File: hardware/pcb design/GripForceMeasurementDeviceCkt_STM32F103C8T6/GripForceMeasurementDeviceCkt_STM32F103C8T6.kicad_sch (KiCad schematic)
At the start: 25 parts, among them J1 Conn_01x03, P1 USB_C_Plug_USB2.0, U1 STM32F103C8Tx, U2 FT232RL, Y1 8MHz

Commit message: initial design of schemetic has completed
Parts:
- removed J1: Conn_01x03, symbol Connector_Generic:Conn_01x03
- added C15, C16, C17, C18, C19, C20, C21, C22, C23, C24: 100n, Capacitor_SMD:C_0603_1608Metric, symbol Device:C
- added J1, J10, J11, J12, J13, J5, J6, J7, J8, J9: Conn_01x32, Connector_FFC-FPC:TE_3-1734839-2_1x32-1MP_P0.5mm_Horizontal, symbol Connector_Generic:Conn_01x32
- added J2: Conn_01x03, Connector_PinHeader_2.54mm:PinHeader_1x03_P2.54mm_Vertical, symbol Connector_Generic:Conn_01x03
- added J3: Conn_01x04, Connector_PinHeader_2.54mm:PinHeader_1x04_P2.54mm_Vertical, symbol Connector_Generic:Conn_01x04
- added J4: Conn_02x03_CC, Connector_PinHeader_2.54mm:PinHeader_2x03_P2.54mm_Vertical, symbol Connector_Generic:Conn_02x03_Counter_Clockwise
- added R4: 330R, Resistor_THT:R_Axial_DIN0207_L6.3mm_D2.5mm_P7.62mm_Horizontal, symbol Device:R
- added RV1: 500k, Potentiometer_THT:Potentiometer_Bourns_3296W_Vertical, symbol Device:R_Potentiometer
- added U10, U11, U12, U13, U3, U4, U6, U7, U8, U9: ADG732BSUZ, Package_QFP:TQFP-48_7x7mm_P0.5mm, symbol ADG732BSUZ:ADG732BSUZ
- added U5: LM358, Package_SO:SO-8_3.9x4.9mm_P1.27mm, symbol Amplifier_Operational:LM358
- C1, C11, C14, C2, C3, C4, C5, C6, C7, C8: footprint (none) -> Capacitor_SMD:C_0603_1608Metric
- C10, C9: footprint (none) -> Capacitor_SMD:C_0402_1005Metric
- C12, C13: footprint (none) -> Capacitor_SMD:C_1206_3216Metric
- D1: footprint Diode_THT:D_DO-41_SOD81_P10.16mm_Horizontal -> Diode_SMD:D_MicroMELF
- FB1, L1: footprint (none) -> Inductor_SMD:L_0805_2012Metric
- P1: footprint (none) -> Connector_USB:USB_C_Receptacle_Amphenol_12401610E4-2A
- R1, R2, R3: footprint (none) -> Resistor_SMD:R_0603_1608Metric
- Y1: footprint (none) -> Crystal:Crystal_HC49-4H_Vertical
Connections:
- net +3.3V: now also J3.1 (Pin_1), J4.1 (Pin_1), J4.6 (Pin_6)
- net +5V: now also C15.1, C16.1, C17.1, C18.1, C19.1, C20.1, C21.1, C22.1, C23.1, C24.1, U10.13 (VDD), U10.14 (VDD)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
- net GND: now also C15.2, C16.2, C17.2, C18.2, C19.2, C20.2, C21.2, C22.2, C23.2, C24.2, J3.4 (Pin_4), J4.3 (Pin_3)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
- net SW_BOOT0: now also J4.5 (Pin_5)
- net ADC: now reaches U1.10 (PA0)
- net ADC: now also J2.2 (Pin_2)
- net COL_SEL_R_3: now reaches U1.11 (PA1)
- net COL_SEL_R_3: now also U12.20 (~{CS})
- net COL_SEL_R_4: now reaches U1.12 (PA2)
- net COL_SEL_R_4: now also U13.20 (~{CS})
- net GYRO_SELECT: now reaches U1.13 (PA3)
- net NSS: now reaches U1.14 (PA4)
- net SCK: now reaches U1.15 (PA5)
- net MISO: now reaches U1.16 (PA6)
- net MOSI: now reaches U1.17 (PA7)
- net ROW_SEL_L: now reaches U1.18 (PB0)
- net ROW_SEL_L: now also U3.20 (~{CS})
- net ROW_SEL_R: now reaches U1.19 (PB1)
- net ROW_SEL_R: now also U4.20 (~{CS})
- net BOOT1: now reaches U1.20 (PB2)
- net BOOT1: now also J4.2 (Pin_2)
- net COL_SEL_L_1: now reaches U1.21 (PB10)
- net COL_SEL_L_1: now also U6.20 (~{CS})
- net COL_SEL_L_2: now reaches U1.22 (PB11)
- net COL_SEL_L_2: now also U7.20 (~{CS})
- net COL_SEL_L_3: now reaches U1.25 (PB12)
- net COL_SEL_L_3: now also U8.20 (~{CS})
- net COL_SEL_L_4: now reaches U1.26 (PB13)
- net COL_SEL_L_4: now also U9.20 (~{CS})
- net COL_SEL_R_1: now reaches U1.27 (PB14)
- net COL_SEL_R_1: now also U10.20 (~{CS})
- net COL_SEL_R_2: now reaches U1.28 (PB15)
- net COL_SEL_R_2: now also U11.20 (~{CS})
- net ESP_SELECT: now reaches U1.29 (PA8)
- net at U1.34 (PA13): now also J3.2 (Pin_2)
- net at U1.37 (PA14): now also J3.3 (Pin_3)
- net ADG_WR: now reaches U1.39 (PB3)
- net ADG_WR: now also U10.21 (~{WR}), U11.21 (~{WR}), U12.21 (~{WR}), U13.21 (~{WR}), U3.21 (~{WR}), U4.21 (~{WR}), U6.21 (~{WR}), U7.21 (~{WR}), U8.21 (~{WR}), U9.21 (~{WR})
- net ADG_EN: now reaches U1.40 (PB4)
- net ADG_EN: now also U10.22 (~{EN}), U11.22 (~{EN}), U12.22 (~{EN}), U13.22 (~{EN}), U3.22 (~{EN}), U4.22 (~{EN}), U6.22 (~{EN}), U7.22 (~{EN}), U8.22 (~{EN}), U9.22 (~{EN})
- net L0: now reaches U1.41 (PB5)
- net L0: now also U10.15 (A0), U11.15 (A0), U12.15 (A0), U13.15 (A0), U3.15 (A0), U4.15 (A0), U6.15 (A0), U7.15 (A0), U8.15 (A0), U9.15 (A0)
- net L1: now reaches U1.42 (PB6)
- net L1: now also U10.16 (A1), U11.16 (A1), U12.16 (A1), U13.16 (A1), U3.16 (A1), U4.16 (A1), U6.16 (A1), U7.16 (A1), U8.16 (A1), U9.16 (A1)
- net L2: now reaches U1.43 (PB7)
- net L2: now also U10.17 (A2), U11.17 (A2), U12.17 (A2), U13.17 (A2), U3.17 (A2), U4.17 (A2), U6.17 (A2), U7.17 (A2), U8.17 (A2), U9.17 (A2)
- net L3: now reaches U1.45 (PB8)
- net L3: now also U10.18 (A3), U11.18 (A3), U12.18 (A3), U13.18 (A3), U3.18 (A3), U4.18 (A3), U6.18 (A3), U7.18 (A3), U8.18 (A3), U9.18 (A3)
- net L4: now reaches U1.46 (PB9)
- net L4: now also U10.19 (A4), U11.19 (A4), U12.19 (A4), U13.19 (A4), U3.19 (A4), U4.19 (A4), U6.19 (A4), U7.19 (A4), U8.19 (A4), U9.19 (A4)
- new net: J2.1 (Pin_1), RV1.1, U5.7
- new net: RV1.2, U5.6 (-)
- new net: J2.3 (Pin_3), U5.1, U5.2 (-), U5.5 (+)
- new net COL_L_1.S1: J5.32 (Pin_32), U6.12 (S1)
- new net COL_L_1.S10: J5.23 (Pin_23), U6.3 (S10)
- new net COL_L_1.S11: J5.22 (Pin_22), U6.2 (S11)
- new net COL_L_1.S12: J5.21 (Pin_21), U6.1 (S12)
- new net COL_L_1.S13: J5.20 (Pin_20), U6.48 (S13)
- new net COL_L_1.S14: J5.19 (Pin_19), U6.47 (S14)
- new net COL_L_1.S15: J5.18 (Pin_18), U6.46 (S15)
- new net COL_L_1.S16: J5.17 (Pin_17), U6.45 (S16)
- new net COL_L_1.S17: J5.1 (Pin_1), U6.25 (S17)
- new net COL_L_1.S18: J5.2 (Pin_2), U6.26 (S18)
- new net COL_L_1.S19: J5.3 (Pin_3), U6.27 (S19)
- new net COL_L_1.S2: J5.31 (Pin_31), U6.11 (S2)
- new net COL_L_1.S20: J5.4 (Pin_4), U6.28 (S20)
- new net COL_L_1.S21: J5.5 (Pin_5), U6.29 (S21)
- new net COL_L_1.S22: J5.6 (Pin_6), U6.30 (S22)
- new net COL_L_1.S23: J5.7 (Pin_7), U6.31 (S23)
- new net COL_L_1.S24: J5.8 (Pin_8), U6.32 (S24)
- new net COL_L_1.S25: J5.9 (Pin_9), U6.33 (S25)
- new net COL_L_1.S26: J5.10 (Pin_10), U6.34 (S26)
- new net COL_L_1.S27: J5.11 (Pin_11), U6.35 (S27)
- new net COL_L_1.S28: J5.12 (Pin_12), U6.36 (S28)
- new net COL_L_1.S29: J5.13 (Pin_13), U6.37 (S29)
- new net COL_L_1.S3: J5.30 (Pin_30), U6.10 (S3)
- new net COL_L_1.S30: J5.14 (Pin_14), U6.38 (S30)
- new net COL_L_1.S31: J5.15 (Pin_15), U6.39 (S31)
- new net COL_L_1.S32: J5.16 (Pin_16), U6.40 (S32)
- new net COL_L_1.S4: J5.29 (Pin_29), U6.9 (S4)
- new net COL_L_1.S5: J5.28 (Pin_28), U6.8 (S5)
- new net COL_L_1.S6: J5.27 (Pin_27), U6.7 (S6)
- new net COL_L_1.S7: J5.26 (Pin_26), U6.6 (S7)
- new net COL_L_1.S8: J5.25 (Pin_25), U6.5 (S8)
- new net COL_L_1.S9: J5.24 (Pin_24), U6.4 (S9)
- new net COL_L_2.S1: J6.1 (Pin_1), U7.12 (S1)
- new net COL_L_2.S10: J6.10 (Pin_10), U7.3 (S10)
- new net COL_L_2.S11: J6.11 (Pin_11), U7.2 (S11)
- new net COL_L_2.S12: J6.12 (Pin_12), U7.1 (S12)
- new net COL_L_2.S13: J6.13 (Pin_13), U7.48 (S13)
- new net COL_L_2.S14: J6.14 (Pin_14), U7.47 (S14)
- new net COL_L_2.S15: J6.15 (Pin_15), U7.46 (S15)
- new net COL_L_2.S16: J6.16 (Pin_16), U7.45 (S16)
- new net COL_L_2.S17: J6.32 (Pin_32), U7.25 (S17)
- new net COL_L_2.S18: J6.31 (Pin_31), U7.26 (S18)
- new net COL_L_2.S19: J6.30 (Pin_30), U7.27 (S19)
- new net COL_L_2.S2: J6.2 (Pin_2), U7.11 (S2)
- new net COL_L_2.S20: J6.29 (Pin_29), U7.28 (S20)
- new net COL_L_2.S21: J6.28 (Pin_28), U7.29 (S21)
- new net COL_L_2.S22: J6.27 (Pin_27), U7.30 (S22)
- new net COL_L_2.S23: J6.26 (Pin_26), U7.31 (S23)
- new net COL_L_2.S24: J6.25 (Pin_25), U7.32 (S24)
- new net COL_L_2.S25: J6.24 (Pin_24), U7.33 (S25)
- new net COL_L_2.S26: J6.23 (Pin_23), U7.34 (S26)
- new net COL_L_2.S27: J6.22 (Pin_22), U7.35 (S27)
- new net COL_L_2.S28: J6.21 (Pin_21), U7.36 (S28)
- new net COL_L_2.S29: J6.20 (Pin_20), U7.37 (S29)
- new net COL_L_2.S3: J6.3 (Pin_3), U7.10 (S3)
- new net COL_L_2.S30: J6.19 (Pin_19), U7.38 (S30)
- new net COL_L_2.S31: J6.18 (Pin_18), U7.39 (S31)
- new net COL_L_2.S32: J6.17 (Pin_17), U7.40 (S32)
- new net COL_L_2.S4: J6.4 (Pin_4), U7.9 (S4)
- new net COL_L_2.S5: J6.5 (Pin_5), U7.8 (S5)
- new net COL_L_2.S6: J6.6 (Pin_6), U7.7 (S6)
- new net COL_L_2.S7: J6.7 (Pin_7), U7.6 (S7)
- new net COL_L_2.S8: J6.8 (Pin_8), U7.5 (S8)
- new net COL_L_2.S9: J6.9 (Pin_9), U7.4 (S9)
- new net COL_L_3.S1: J7.1 (Pin_1), U8.12 (S1)
- new net COL_L_3.S10: J7.10 (Pin_10), U8.3 (S10)
- new net COL_L_3.S11: J7.11 (Pin_11), U8.2 (S11)
- new net COL_L_3.S12: J7.12 (Pin_12), U8.1 (S12)
- new net COL_L_3.S13: J7.13 (Pin_13), U8.48 (S13)
- new net COL_L_3.S14: J7.14 (Pin_14), U8.47 (S14)
- new net COL_L_3.S15: J7.15 (Pin_15), U8.46 (S15)
- new net COL_L_3.S16: J7.16 (Pin_16), U8.45 (S16)
- new net COL_L_3.S17: J7.32 (Pin_32), U8.25 (S17)
- new net COL_L_3.S18: J7.31 (Pin_31), U8.26 (S18)
- new net COL_L_3.S19: J7.30 (Pin_30), U8.27 (S19)
- new net COL_L_3.S2: J7.2 (Pin_2), U8.11 (S2)
- new net COL_L_3.S20: J7.29 (Pin_29), U8.28 (S20)
- new net COL_L_3.S21: J7.28 (Pin_28), U8.29 (S21)
- new net COL_L_3.S22: J7.27 (Pin_27), U8.30 (S22)
- new net COL_L_3.S23: J7.26 (Pin_26), U8.31 (S23)
- new net COL_L_3.S24: J7.25 (Pin_25), U8.32 (S24)
- new net COL_L_3.S25: J7.24 (Pin_24), U8.33 (S25)
- new net COL_L_3.S26: J7.23 (Pin_23), U8.34 (S26)
- new net COL_L_3.S27: J7.22 (Pin_22), U8.35 (S27)
- new net COL_L_3.S28: J7.21 (Pin_21), U8.36 (S28)
- new net COL_L_3.S29: J7.20 (Pin_20), U8.37 (S29)
- new net COL_L_3.S3: J7.3 (Pin_3), U8.10 (S3)
- new net COL_L_3.S30: J7.19 (Pin_19), U8.38 (S30)
- new net COL_L_3.S31: J7.18 (Pin_18), U8.39 (S31)
- new net COL_L_3.S32: J7.17 (Pin_17), U8.40 (S32)
- new net COL_L_3.S4: J7.4 (Pin_4), U8.9 (S4)
- new net COL_L_3.S5: J7.5 (Pin_5), U8.8 (S5)
- new net COL_L_3.S6: J7.6 (Pin_6), U8.7 (S6)
- new net COL_L_3.S7: J7.7 (Pin_7), U8.6 (S7)
- new net COL_L_3.S8: J7.8 (Pin_8), U8.5 (S8)
- new net COL_L_3.S9: J7.9 (Pin_9), U8.4 (S9)
- new net COL_L_4.S1: J8.1 (Pin_1), U9.12 (S1)
- new net COL_L_4.S10: J8.10 (Pin_10), U9.3 (S10)
- new net COL_L_4.S11: J8.11 (Pin_11), U9.2 (S11)
- new net COL_L_4.S12: J8.12 (Pin_12), U9.1 (S12)
- new net COL_L_4.S13: J8.13 (Pin_13), U9.48 (S13)
- new net COL_L_4.S14: J8.14 (Pin_14), U9.47 (S14)
- new net COL_L_4.S15: J8.15 (Pin_15), U9.46 (S15)
- new net COL_L_4.S16: J8.16 (Pin_16), U9.45 (S16)
- new net COL_L_4.S17: J8.32 (Pin_32), U9.25 (S17)
- new net COL_L_4.S18: J8.31 (Pin_31), U9.26 (S18)
- new net COL_L_4.S19: J8.30 (Pin_30), U9.27 (S19)
- new net COL_L_4.S2: J8.2 (Pin_2), U9.11 (S2)
- new net COL_L_4.S20: J8.29 (Pin_29), U9.28 (S20)
- new net COL_L_4.S21: J8.28 (Pin_28), U9.29 (S21)
- new net COL_L_4.S22: J8.27 (Pin_27), U9.30 (S22)
- new net COL_L_4.S23: J8.26 (Pin_26), U9.31 (S23)
- new net COL_L_4.S24: J8.25 (Pin_25), U9.32 (S24)
- new net COL_L_4.S25: J8.24 (Pin_24), U9.33 (S25)
- new net COL_L_4.S26: J8.23 (Pin_23), U9.34 (S26)
- new net COL_L_4.S27: J8.22 (Pin_22), U9.35 (S27)
- new net COL_L_4.S28: J8.21 (Pin_21), U9.36 (S28)
- new net COL_L_4.S29: J8.20 (Pin_20), U9.37 (S29)
- new net COL_L_4.S3: J8.3 (Pin_3), U9.10 (S3)
- new net COL_L_4.S30: J8.19 (Pin_19), U9.38 (S30)
- new net COL_L_4.S31: J8.18 (Pin_18), U9.39 (S31)
- new net COL_L_4.S32: J8.17 (Pin_17), U9.40 (S32)
- new net COL_L_4.S4: J8.4 (Pin_4), U9.9 (S4)
- new net COL_L_4.S5: J8.5 (Pin_5), U9.8 (S5)
- new net COL_L_4.S6: J8.6 (Pin_6), U9.7 (S6)
- new net COL_L_4.S7: J8.7 (Pin_7), U9.6 (S7)
- new net COL_L_4.S8: J8.8 (Pin_8), U9.5 (S8)
- new net COL_L_4.S9: J8.9 (Pin_9), U9.4 (S9)
- new net COL_R_1.S1: J9.1 (Pin_1), U10.12 (S1)
- new net COL_R_1.S10: J9.10 (Pin_10), U10.3 (S10)
- new net COL_R_1.S11: J9.11 (Pin_11), U10.2 (S11)
- new net COL_R_1.S12: J9.12 (Pin_12), U10.1 (S12)
- new net COL_R_1.S13: J9.13 (Pin_13), U10.48 (S13)
- new net COL_R_1.S14: J9.14 (Pin_14), U10.47 (S14)
- new net COL_R_1.S15: J9.15 (Pin_15), U10.46 (S15)
- new net COL_R_1.S16: J9.16 (Pin_16), U10.45 (S16)
- new net COL_R_1.S17: J9.32 (Pin_32), U10.25 (S17)
- new net COL_R_1.S18: J9.31 (Pin_31), U10.26 (S18)
- new net COL_R_1.S19: J9.30 (Pin_30), U10.27 (S19)
- new net COL_R_1.S2: J9.2 (Pin_2), U10.11 (S2)
- new net COL_R_1.S20: J9.29 (Pin_29), U10.28 (S20)
- new net COL_R_1.S21: J9.28 (Pin_28), U10.29 (S21)
- new net COL_R_1.S22: J9.27 (Pin_27), U10.30 (S22)
- new net COL_R_1.S23: J9.26 (Pin_26), U10.31 (S23)
- new net COL_R_1.S24: J9.25 (Pin_25), U10.32 (S24)
- new net COL_R_1.S25: J9.24 (Pin_24), U10.33 (S25)
- new net COL_R_1.S26: J9.23 (Pin_23), U10.34 (S26)
- new net COL_R_1.S27: J9.22 (Pin_22), U10.35 (S27)
- new net COL_R_1.S28: J9.21 (Pin_21), U10.36 (S28)
- new net COL_R_1.S29: J9.20 (Pin_20), U10.37 (S29)
- new net COL_R_1.S3: J9.3 (Pin_3), U10.10 (S3)
- new net COL_R_1.S30: J9.19 (Pin_19), U10.38 (S30)
- new net COL_R_1.S31: J9.18 (Pin_18), U10.39 (S31)
- new net COL_R_1.S32: J9.17 (Pin_17), U10.40 (S32)
- new net COL_R_1.S4: J9.4 (Pin_4), U10.9 (S4)
- new net COL_R_1.S5: J9.5 (Pin_5), U10.8 (S5)
- new net COL_R_1.S6: J9.6 (Pin_6), U10.7 (S6)
- new net COL_R_1.S7: J9.7 (Pin_7), U10.6 (S7)
- new net COL_R_1.S8: J9.8 (Pin_8), U10.5 (S8)
- new net COL_R_1.S9: J9.9 (Pin_9), U10.4 (S9)
- new net COL_R_2.S1: J11.1 (Pin_1), U11.12 (S1)
- new net COL_R_2.S10: J11.10 (Pin_10), U11.3 (S10)
- new net COL_R_2.S11: J11.11 (Pin_11), U11.2 (S11)
- new net COL_R_2.S12: J11.12 (Pin_12), U11.1 (S12)
- new net COL_R_2.S13: J11.13 (Pin_13), U11.48 (S13)
- new net COL_R_2.S14: J11.14 (Pin_14), U11.47 (S14)
- new net COL_R_2.S15: J11.15 (Pin_15), U11.46 (S15)
- new net COL_R_2.S16: J11.16 (Pin_16), U11.45 (S16)
- new net COL_R_2.S17: J11.32 (Pin_32), U11.25 (S17)
- new net COL_R_2.S18: J11.31 (Pin_31), U11.26 (S18)
- new net COL_R_2.S19: J11.30 (Pin_30), U11.27 (S19)
- new net COL_R_2.S2: J11.2 (Pin_2), U11.11 (S2)
- new net COL_R_2.S20: J11.29 (Pin_29), U11.28 (S20)
- new net COL_R_2.S21: J11.28 (Pin_28), U11.29 (S21)
- new net COL_R_2.S22: J11.27 (Pin_27), U11.30 (S22)
- new net COL_R_2.S23: J11.26 (Pin_26), U11.31 (S23)
- new net COL_R_2.S24: J11.25 (Pin_25), U11.32 (S24)
- new net COL_R_2.S25: J11.24 (Pin_24), U11.33 (S25)
- new net COL_R_2.S26: J11.23 (Pin_23), U11.34 (S26)
- new net COL_R_2.S27: J11.22 (Pin_22), U11.35 (S27)
- new net COL_R_2.S28: J11.21 (Pin_21), U11.36 (S28)
- new net COL_R_2.S29: J11.20 (Pin_20), U11.37 (S29)
- new net COL_R_2.S3: J11.3 (Pin_3), U11.10 (S3)
- new net COL_R_2.S30: J11.19 (Pin_19), U11.38 (S30)
- new net COL_R_2.S31: J11.18 (Pin_18), U11.39 (S31)
- new net COL_R_2.S32: J11.17 (Pin_17), U11.40 (S32)
- new net COL_R_2.S4: J11.4 (Pin_4), U11.9 (S4)
- new net COL_R_2.S5: J11.5 (Pin_5), U11.8 (S5)
- new net COL_R_2.S6: J11.6 (Pin_6), U11.7 (S6)
- new net COL_R_2.S7: J11.7 (Pin_7), U11.6 (S7)
- new net COL_R_2.S8: J11.8 (Pin_8), U11.5 (S8)
- new net COL_R_2.S9: J11.9 (Pin_9), U11.4 (S9)
- new net COL_R_3.S1: J12.1 (Pin_1), U12.12 (S1)
- new net COL_R_3.S10: J12.10 (Pin_10), U12.3 (S10)
- new net COL_R_3.S11: J12.11 (Pin_11), U12.2 (S11)
- new net COL_R_3.S12: J12.12 (Pin_12), U12.1 (S12)
- new net COL_R_3.S13: J12.13 (Pin_13), U12.48 (S13)
- new net COL_R_3.S14: J12.14 (Pin_14), U12.47 (S14)
- new net COL_R_3.S15: J12.15 (Pin_15), U12.46 (S15)
- new net COL_R_3.S16: J12.16 (Pin_16), U12.45 (S16)
- new net COL_R_3.S17: J12.32 (Pin_32), U12.25 (S17)
- new net COL_R_3.S18: J12.31 (Pin_31), U12.26 (S18)
- new net COL_R_3.S19: J12.30 (Pin_30), U12.27 (S19)
- new net COL_R_3.S2: J12.2 (Pin_2), U12.11 (S2)
- new net COL_R_3.S20: J12.29 (Pin_29), U12.28 (S20)
- new net COL_R_3.S21: J12.28 (Pin_28), U12.29 (S21)
- new net COL_R_3.S22: J12.27 (Pin_27), U12.30 (S22)
- new net COL_R_3.S23: J12.26 (Pin_26), U12.31 (S23)
- new net COL_R_3.S24: J12.25 (Pin_25), U12.32 (S24)
- new net COL_R_3.S25: J12.24 (Pin_24), U12.33 (S25)
- new net COL_R_3.S26: J12.23 (Pin_23), U12.34 (S26)
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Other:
- note added: "Serial Wire Debugger (SWD)"
- company: (none) -> University of Regina
- title: (none) -> Girp Force Measurement Circuit. V - 2.0.0
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
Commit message: complete schemetic design. working on PCB
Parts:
- removed J1, J10, J6, J7: Conn_01x32, Connector_FFC-FPC:TE_3-1734839-2_1x32-1MP_P0.5mm_Horizontal, symbol Connector_Generic:Conn_01x32
- added J1: RX_Conn, Connector_PinHeader_2.54mm:PinHeader_1x03_P2.54mm_Vertical, symbol Connector_Generic:Conn_01x03
- added J14, J15, J16, J17: Conn_01x32, Connector_FFC-FPC:Hirose_FH12-32S-0.5SH_1x32-1MP_P0.50mm_Horizontal, symbol Connector_Generic:Conn_01x32
- added J19: Power_Conn, Connector_PinHeader_2.54mm:PinHeader_1x03_P2.54mm_Vertical, symbol Connector_Generic:Conn_01x03
- added J3: TX_Conn, Connector_PinHeader_2.54mm:PinHeader_1x03_P2.54mm_Vertical, symbol Connector_Generic:Conn_01x03
- added J4: Bluetooth_Module_HLK_B40_(Customized), Connector_PinSocket_2.54mm:PinSocket_1x06_P2.54mm_Vertical, symbol Connector_Generic:Conn_01x06
- added J7: Gyro_Sensor_ICM_20948_SparkFun_Module, Connector_PinSocket_2.54mm:PinSocket_1x06_P2.54mm_Vertical, symbol Connector_Generic:Conn_01x06
- added U1: ESP32-C3-Mini, RF_WiFi:ESP32-C3-Mini-through-hole, symbol RF_WiFi:ESP32-C3-Mini
- J10: renamed from J5; footprint Connector_FFC-FPC:TE_3-1734839-2_1x32-1MP_P0.5mm_Horizontal -> Connector_FFC-FPC:Hirose_FH12-32S-0.5SH_1x32-1MP_P0.50mm_Horizontal
- J11, J12, J13, J8, J9: footprint Connector_FFC-FPC:TE_3-1734839-2_1x32-1MP_P0.5mm_Horizontal -> Connector_FFC-FPC:Hirose_FH12-32S-0.5SH_1x32-1MP_P0.50mm_Horizontal
- J2: renamed from J4; value Conn_02x03_CC -> Boot_Conn
- J5: renamed from J3; value Conn_01x04 -> SWD
- renumbered C14 to C1, C11 to C10, C12 to C11, C8 to C12, C9 to C13, C10 to C14, C20 to C15, C15 to C16, C1 to C2, C24 to C20, C22 to C21, C23 to C22, C21 to C23, C16 to C24, C2 to C3, C3 to C4, C4 to C5, C5 to C6, C6 to C7, C7 to C8, C13 to C9, J2 to J6, R2 to R1, R1 to R2, U13 to U10, U10 to U13, U4 to U14, U5 to U3, U1 to U4, U9 to U5, U3 to U6, U6 to U7, U7 to U8, U8 to U9
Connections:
- net +5V: now also J4.5 (Pin_5), J7.1 (Pin_1), U1.1 (5V)
- net COL_L_2.S1: now also J11.32 (Pin_32)
- net COL_L_2.S10: now also J11.23 (Pin_23)
- net COL_L_2.S11: now also J11.22 (Pin_22)
- net COL_L_2.S12: now also J11.21 (Pin_21)
- net COL_L_2.S13: now also J11.20 (Pin_20)
- net COL_L_2.S14: now also J11.19 (Pin_19)
- net COL_L_2.S15: now also J11.18 (Pin_18)
- net COL_L_2.S16: now also J11.17 (Pin_17)
- net COL_L_2.S17: now also J11.1 (Pin_1)
- net COL_L_2.S18: now also J11.2 (Pin_2)
- net COL_L_2.S19: now also J11.3 (Pin_3)
- net COL_L_2.S2: now also J11.31 (Pin_31)
- net COL_L_2.S20: now also J11.4 (Pin_4)
- net COL_L_2.S21: now also J11.5 (Pin_5)
- net COL_L_2.S22: now also J11.6 (Pin_6)
- net COL_L_2.S23: now also J11.7 (Pin_7)
- net COL_L_2.S24: now also J11.8 (Pin_8)
- net COL_L_2.S25: now also J11.9 (Pin_9)
- net COL_L_2.S26: now also J11.10 (Pin_10)
- net COL_L_2.S27: now also J11.11 (Pin_11)
- net COL_L_2.S28: now also J11.12 (Pin_12)
- net COL_L_2.S29: now also J11.13 (Pin_13)
- net COL_L_2.S3: now also J11.30 (Pin_30)
- net COL_L_2.S30: now also J11.14 (Pin_14)
- net COL_L_2.S31: now also J11.15 (Pin_15)
- net COL_L_2.S32: now also J11.16 (Pin_16)
- net COL_L_2.S4: now also J11.29 (Pin_29)
- net COL_L_2.S5: now also J11.28 (Pin_28)
- net COL_L_2.S6: now also J11.27 (Pin_27)
- net COL_L_2.S7: now also J11.26 (Pin_26)
- net COL_L_2.S8: now also J11.25 (Pin_25)
- net COL_L_2.S9: now also J11.24 (Pin_24)
- net COL_L_3.S1: now also J12.32 (Pin_32)
- net COL_L_3.S10: now also J12.23 (Pin_23)
- net COL_L_3.S11: now also J12.22 (Pin_22)
- net COL_L_3.S12: now also J12.21 (Pin_21)
- net COL_L_3.S13: now also J12.20 (Pin_20)
- net COL_L_3.S14: now also J12.19 (Pin_19)
- net COL_L_3.S15: now also J12.18 (Pin_18)
- net COL_L_3.S16: now also J12.17 (Pin_17)
- net COL_L_3.S17: now also J12.1 (Pin_1)
- net COL_L_3.S18: now also J12.2 (Pin_2)
- net COL_L_3.S19: now also J12.3 (Pin_3)
- net COL_L_3.S2: now also J12.31 (Pin_31)
- net COL_L_3.S20: now also J12.4 (Pin_4)
- net COL_L_3.S21: now also J12.5 (Pin_5)
- net COL_L_3.S22: now also J12.6 (Pin_6)
- net COL_L_3.S23: now also J12.7 (Pin_7)
- net COL_L_3.S24: now also J12.8 (Pin_8)
- net COL_L_3.S25: now also J12.9 (Pin_9)
- net COL_L_3.S26: now also J12.10 (Pin_10)
- net COL_L_3.S27: now also J12.11 (Pin_11)
- net COL_L_3.S28: now also J12.12 (Pin_12)
- net COL_L_3.S29: now also J12.13 (Pin_13)
- net COL_L_3.S3: now also J12.30 (Pin_30)
- net COL_L_3.S30: now also J12.14 (Pin_14)
- net COL_L_3.S31: now also J12.15 (Pin_15)
- net COL_L_3.S32: now also J12.16 (Pin_16)
- net COL_L_3.S4: now also J12.29 (Pin_29)
- net COL_L_3.S5: now also J12.28 (Pin_28)
- net COL_L_3.S6: now also J12.27 (Pin_27)
- net COL_L_3.S7: now also J12.26 (Pin_26)
- net COL_L_3.S8: now also J12.25 (Pin_25)
- net COL_L_3.S9: now also J12.24 (Pin_24)
- net COL_L_4.S1: now also J8.32 (Pin_32); no longer J8.1 (Pin_1)
- net COL_L_4.S10: now also J8.23 (Pin_23); no longer J8.10 (Pin_10)
- net COL_L_4.S11: now also J8.22 (Pin_22); no longer J8.11 (Pin_11)
- net COL_L_4.S12: now also J8.21 (Pin_21); no longer J8.12 (Pin_12)
- net COL_L_4.S13: now also J8.20 (Pin_20); no longer J8.13 (Pin_13)
- net COL_L_4.S14: now also J8.19 (Pin_19); no longer J8.14 (Pin_14)
- net COL_L_4.S15: now also J8.18 (Pin_18); no longer J8.15 (Pin_15)
- net COL_L_4.S16: now also J8.17 (Pin_17); no longer J8.16 (Pin_16)
- net COL_L_4.S17: now also J8.1 (Pin_1); no longer J8.32 (Pin_32)
- net COL_L_4.S18: now also J8.2 (Pin_2); no longer J8.31 (Pin_31)
- net COL_L_4.S19: now also J8.3 (Pin_3); no longer J8.30 (Pin_30)
- net COL_L_4.S2: now also J8.31 (Pin_31); no longer J8.2 (Pin_2)
- net COL_L_4.S20: now also J8.4 (Pin_4); no longer J8.29 (Pin_29)
- net COL_L_4.S21: now also J8.5 (Pin_5); no longer J8.28 (Pin_28)
- net COL_L_4.S22: now also J8.6 (Pin_6); no longer J8.27 (Pin_27)
- net COL_L_4.S23: now also J8.7 (Pin_7); no longer J8.26 (Pin_26)
- net COL_L_4.S24: now also J8.8 (Pin_8); no longer J8.25 (Pin_25)
- net COL_L_4.S25: now also J8.9 (Pin_9); no longer J8.24 (Pin_24)
- net COL_L_4.S26: now also J8.10 (Pin_10); no longer J8.23 (Pin_23)
- net COL_L_4.S27: now also J8.11 (Pin_11); no longer J8.22 (Pin_22)
- net COL_L_4.S28: now also J8.12 (Pin_12); no longer J8.21 (Pin_21)
- net COL_L_4.S29: now also J8.13 (Pin_13); no longer J8.20 (Pin_20)
- net COL_L_4.S3: now also J8.30 (Pin_30); no longer J8.3 (Pin_3)
- net COL_L_4.S30: now also J8.14 (Pin_14); no longer J8.19 (Pin_19)
- net COL_L_4.S31: now also J8.15 (Pin_15); no longer J8.18 (Pin_18)
- net COL_L_4.S32: now also J8.16 (Pin_16); no longer J8.17 (Pin_17)
- net COL_L_4.S4: now also J8.29 (Pin_29); no longer J8.4 (Pin_4)
- net COL_L_4.S5: now also J8.28 (Pin_28); no longer J8.5 (Pin_5)
- net COL_L_4.S6: now also J8.27 (Pin_27); no longer J8.6 (Pin_6)
- net COL_L_4.S7: now also J8.26 (Pin_26); no longer J8.7 (Pin_7)
- net COL_L_4.S8: now also J8.25 (Pin_25); no longer J8.8 (Pin_8)
- net COL_L_4.S9: now also J8.24 (Pin_24); no longer J8.9 (Pin_9)
- net COL_R_1.S1: now also J14.32 (Pin_32); no longer J9.1 (Pin_1)
- net COL_R_1.S10: now also J14.23 (Pin_23); no longer J9.10 (Pin_10)
- net COL_R_1.S11: now also J14.22 (Pin_22); no longer J9.11 (Pin_11)
- net COL_R_1.S12: now also J14.21 (Pin_21); no longer J9.12 (Pin_12)
- net COL_R_1.S13: now also J14.20 (Pin_20); no longer J9.13 (Pin_13)
- net COL_R_1.S14: now also J14.19 (Pin_19); no longer J9.14 (Pin_14)
- net COL_R_1.S15: now also J14.18 (Pin_18); no longer J9.15 (Pin_15)
- net COL_R_1.S16: now also J14.17 (Pin_17); no longer J9.16 (Pin_16)
- net COL_R_1.S17: now also J14.1 (Pin_1); no longer J9.32 (Pin_32)
- net COL_R_1.S18: now also J14.2 (Pin_2); no longer J9.31 (Pin_31)
- net COL_R_1.S19: now also J14.3 (Pin_3); no longer J9.30 (Pin_30)
- net COL_R_1.S2: now also J14.31 (Pin_31); no longer J9.2 (Pin_2)
- net COL_R_1.S20: now also J14.4 (Pin_4); no longer J9.29 (Pin_29)
- net COL_R_1.S21: now also J14.5 (Pin_5); no longer J9.28 (Pin_28)
- net COL_R_1.S22: now also J14.6 (Pin_6); no longer J9.27 (Pin_27)
- net COL_R_1.S23: now also J14.7 (Pin_7); no longer J9.26 (Pin_26)
- net COL_R_1.S24: now also J14.8 (Pin_8); no longer J9.25 (Pin_25)
- net COL_R_1.S25: now also J14.9 (Pin_9); no longer J9.24 (Pin_24)
- net COL_R_1.S26: now also J14.10 (Pin_10); no longer J9.23 (Pin_23)
- net COL_R_1.S27: now also J14.11 (Pin_11); no longer J9.22 (Pin_22)
- net COL_R_1.S28: now also J14.12 (Pin_12); no longer J9.21 (Pin_21)
- net COL_R_1.S29: now also J14.13 (Pin_13); no longer J9.20 (Pin_20)
- net COL_R_1.S3: now also J14.30 (Pin_30); no longer J9.3 (Pin_3)
- net COL_R_1.S30: now also J14.14 (Pin_14); no longer J9.19 (Pin_19)
- net COL_R_1.S31: now also J14.15 (Pin_15); no longer J9.18 (Pin_18)
- net COL_R_1.S32: now also J14.16 (Pin_16); no longer J9.17 (Pin_17)
- net COL_R_1.S4: now also J14.29 (Pin_29); no longer J9.4 (Pin_4)
- net COL_R_1.S5: now also J14.28 (Pin_28); no longer J9.5 (Pin_5)
- net COL_R_1.S6: now also J14.27 (Pin_27); no longer J9.6 (Pin_6)
- net COL_R_1.S7: now also J14.26 (Pin_26); no longer J9.7 (Pin_7)
- net COL_R_1.S8: now also J14.25 (Pin_25); no longer J9.8 (Pin_8)
- net COL_R_1.S9: now also J14.24 (Pin_24); no longer J9.9 (Pin_9)
- net COL_R_2.S1: now also J15.32 (Pin_32); no longer J11.1 (Pin_1)
- net COL_R_2.S10: now also J15.23 (Pin_23); no longer J11.10 (Pin_10)
- net COL_R_2.S11: now also J15.22 (Pin_22); no longer J11.11 (Pin_11)
- net COL_R_2.S12: now also J15.21 (Pin_21); no longer J11.12 (Pin_12)
- net COL_R_2.S13: now also J15.20 (Pin_20); no longer J11.13 (Pin_13)
- net COL_R_2.S14: now also J15.19 (Pin_19); no longer J11.14 (Pin_14)
- net COL_R_2.S15: now also J15.18 (Pin_18); no longer J11.15 (Pin_15)
- net COL_R_2.S16: now also J15.17 (Pin_17); no longer J11.16 (Pin_16)
- net COL_R_2.S17: now also J15.1 (Pin_1); no longer J11.32 (Pin_32)
- net COL_R_2.S18: now also J15.2 (Pin_2); no longer J11.31 (Pin_31)
- net COL_R_2.S19: now also J15.3 (Pin_3); no longer J11.30 (Pin_30)
- net COL_R_2.S2: now also J15.31 (Pin_31); no longer J11.2 (Pin_2)
- net COL_R_2.S20: now also J15.4 (Pin_4); no longer J11.29 (Pin_29)
- net COL_R_2.S21: now also J15.5 (Pin_5); no longer J11.28 (Pin_28)
- net COL_R_2.S22: now also J15.6 (Pin_6); no longer J11.27 (Pin_27)
- net COL_R_2.S23: now also J15.7 (Pin_7); no longer J11.26 (Pin_26)
- net COL_R_2.S24: now also J15.8 (Pin_8); no longer J11.25 (Pin_25)
- net COL_R_2.S25: now also J15.9 (Pin_9); no longer J11.24 (Pin_24)
- net COL_R_2.S26: now also J15.10 (Pin_10); no longer J11.23 (Pin_23)
- net COL_R_2.S27: now also J15.11 (Pin_11); no longer J11.22 (Pin_22)
- net COL_R_2.S28: now also J15.12 (Pin_12); no longer J11.21 (Pin_21)
- net COL_R_2.S29: now also J15.13 (Pin_13); no longer J11.20 (Pin_20)
- net COL_R_2.S3: now also J15.30 (Pin_30); no longer J11.3 (Pin_3)
- net COL_R_2.S30: now also J15.14 (Pin_14); no longer J11.19 (Pin_19)
- net COL_R_2.S31: now also J15.15 (Pin_15); no longer J11.18 (Pin_18)
- net COL_R_2.S32: now also J15.16 (Pin_16); no longer J11.17 (Pin_17)
- net COL_R_2.S4: now also J15.29 (Pin_29); no longer J11.4 (Pin_4)
- net COL_R_2.S5: now also J15.28 (Pin_28); no longer J11.5 (Pin_5)
- net COL_R_2.S6: now also J15.27 (Pin_27); no longer J11.6 (Pin_6)
- net COL_R_2.S7: now also J15.26 (Pin_26); no longer J11.7 (Pin_7)
- net COL_R_2.S8: now also J15.25 (Pin_25); no longer J11.8 (Pin_8)
- net COL_R_2.S9: now also J15.24 (Pin_24); no longer J11.9 (Pin_9)
- net COL_R_3.S1: now also J16.32 (Pin_32); no longer J12.1 (Pin_1)
- net COL_R_3.S10: now also J16.23 (Pin_23); no longer J12.10 (Pin_10)
- net COL_R_3.S11: now also J16.22 (Pin_22); no longer J12.11 (Pin_11)
- net COL_R_3.S12: now also J16.21 (Pin_21); no longer J12.12 (Pin_12)
- net COL_R_3.S13: now also J16.20 (Pin_20); no longer J12.13 (Pin_13)
- net COL_R_3.S14: now also J16.19 (Pin_19); no longer J12.14 (Pin_14)
- net COL_R_3.S15: now also J16.18 (Pin_18); no longer J12.15 (Pin_15)
- net COL_R_3.S16: now also J16.17 (Pin_17); no longer J12.16 (Pin_16)
- net COL_R_3.S17: now also J16.1 (Pin_1); no longer J12.32 (Pin_32)
- net COL_R_3.S18: now also J16.2 (Pin_2); no longer J12.31 (Pin_31)
- net COL_R_3.S19: now also J16.3 (Pin_3); no longer J12.30 (Pin_30)
- net COL_R_3.S2: now also J16.31 (Pin_31); no longer J12.2 (Pin_2)
- net COL_R_3.S20: now also J16.4 (Pin_4); no longer J12.29 (Pin_29)
- net COL_R_3.S21: now also J16.5 (Pin_5); no longer J12.28 (Pin_28)
- net COL_R_3.S22: now also J16.6 (Pin_6); no longer J12.27 (Pin_27)
- net COL_R_3.S23: now also J16.7 (Pin_7); no longer J12.26 (Pin_26)
- net COL_R_3.S24: now also J16.8 (Pin_8); no longer J12.25 (Pin_25)
- net COL_R_3.S25: now also J16.9 (Pin_9); no longer J12.24 (Pin_24)
- net COL_R_3.S26: now also J16.10 (Pin_10); no longer J12.23 (Pin_23)
- net COL_R_3.S27: now also J16.11 (Pin_11); no longer J12.22 (Pin_22)
- net COL_R_3.S28: now also J16.12 (Pin_12); no longer J12.21 (Pin_21)
- net COL_R_3.S29: now also J16.13 (Pin_13); no longer J12.20 (Pin_20)
- net COL_R_3.S3: now also J16.30 (Pin_30); no longer J12.3 (Pin_3)
- net COL_R_3.S30: now also J16.14 (Pin_14); no longer J12.19 (Pin_19)
- net COL_R_3.S31: now also J16.15 (Pin_15); no longer J12.18 (Pin_18)
- net COL_R_3.S32: now also J16.16 (Pin_16); no longer J12.17 (Pin_17)
- net COL_R_3.S4: now also J16.29 (Pin_29); no longer J12.4 (Pin_4)
- net COL_R_3.S5: now also J16.28 (Pin_28); no longer J12.5 (Pin_5)
- net COL_R_3.S6: now also J16.27 (Pin_27); no longer J12.6 (Pin_6)
- net COL_R_3.S7: now also J16.26 (Pin_26); no longer J12.7 (Pin_7)
- net COL_R_3.S8: now also J16.25 (Pin_25); no longer J12.8 (Pin_8)
- net COL_R_3.S9: now also J16.24 (Pin_24); no longer J12.9 (Pin_9)
- net COL_R_4.S1: now also J13.32 (Pin_32); no longer J13.1 (Pin_1)
- net COL_R_4.S10: now also J13.23 (Pin_23); no longer J13.10 (Pin_10)
- net COL_R_4.S11: now also J13.22 (Pin_22); no longer J13.11 (Pin_11)
- net COL_R_4.S12: now also J13.21 (Pin_21); no longer J13.12 (Pin_12)
- net COL_R_4.S13: now also J13.20 (Pin_20); no longer J13.13 (Pin_13)
- net COL_R_4.S14: now also J13.19 (Pin_19); no longer J13.14 (Pin_14)
- net COL_R_4.S15: now also J13.18 (Pin_18); no longer J13.15 (Pin_15)
- net COL_R_4.S16: now also J13.17 (Pin_17); no longer J13.16 (Pin_16)
- net COL_R_4.S17: now also J13.1 (Pin_1); no longer J13.32 (Pin_32)
- net COL_R_4.S18: now also J13.2 (Pin_2); no longer J13.31 (Pin_31)
- net COL_R_4.S19: now also J13.3 (Pin_3); no longer J13.30 (Pin_30)
- net COL_R_4.S2: now also J13.31 (Pin_31); no longer J13.2 (Pin_2)
- net COL_R_4.S20: now also J13.4 (Pin_4); no longer J13.29 (Pin_29)
- net COL_R_4.S21: now also J13.5 (Pin_5); no longer J13.28 (Pin_28)
- net COL_R_4.S22: now also J13.6 (Pin_6); no longer J13.27 (Pin_27)
- net COL_R_4.S23: now also J13.7 (Pin_7); no longer J13.26 (Pin_26)
- net COL_R_4.S24: now also J13.8 (Pin_8); no longer J13.25 (Pin_25)
- net COL_R_4.S25: now also J13.9 (Pin_9); no longer J13.24 (Pin_24)
- net COL_R_4.S26: now also J13.10 (Pin_10); no longer J13.23 (Pin_23)
- net COL_R_4.S27: now also J13.11 (Pin_11); no longer J13.22 (Pin_22)
- net COL_R_4.S28: now also J13.12 (Pin_12); no longer J13.21 (Pin_21)
- net COL_R_4.S29: now also J13.13 (Pin_13); no longer J13.20 (Pin_20)
- net COL_R_4.S3: now also J13.30 (Pin_30); no longer J13.3 (Pin_3)
- net COL_R_4.S30: now also J13.14 (Pin_14); no longer J13.19 (Pin_19)
- net NSS renamed NSS-STM32
- net SCK renamed SCLK
- new net CS-GYRO: J7.6 (Pin_6), U1.7 (GP3)
- new net RX_BTH: J3.1 (Pin_1), J4.2 (Pin_2), U1.17 (GP20)
- new net RX_USB: J3.3 (Pin_3), U2.5 (RXD)
- new net TX_BTH: J1.1 (Pin_1), J4.3 (Pin_3), U1.18 (GP21)
- new net TX_USB: J1.3 (Pin_3), U2.1 (TXD)
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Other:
- note added: "(Optional: If ESP32 is mounted than No need this Bluetooth Module.)"
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
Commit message: updated PCB design
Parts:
- removed J2: Boot_Conn, Connector_PinHeader_2.54mm:PinHeader_2x03_P2.54mm_Vertical, symbol Connector_Generic:Conn_02x03_Counter_Clockwise
- added J2: Boot Conn, Connector_PinHeader_2.54mm:PinHeader_2x03_P2.54mm_Vertical, symbol Connector_Generic:Conn_02x03_Odd_Even
- added SW1: SW_Push, Button_Switch_SMD:SW_Tactile_SPST_NO_Straight_CK_PTS636Sx25SMTRLFS, symbol Switch:SW_Push
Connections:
- net +3.3V: now also J2.1 (Pin_1), J2.2 (Pin_2)
- net BOOT1: now also J2.3 (Pin_3)
- net GND: now also J2.5 (Pin_5), J2.6 (Pin_6), SW1.1
- net NRST: now also SW1.2
- net SW_BOOT0: now also J2.4 (Pin_4)
- net D+: now reaches P1.A6 (D+), U2.15 (USBD+)
- net D-: now reaches P1.A7 (D-), U2.16 (USBD-)
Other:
- note added: "Hand Grip-force Measurement Device's Circuit"
- moved on the sheet: C12, C13, C14, C2, C3, C4, C5, C6, C7, C8, FB1, J1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

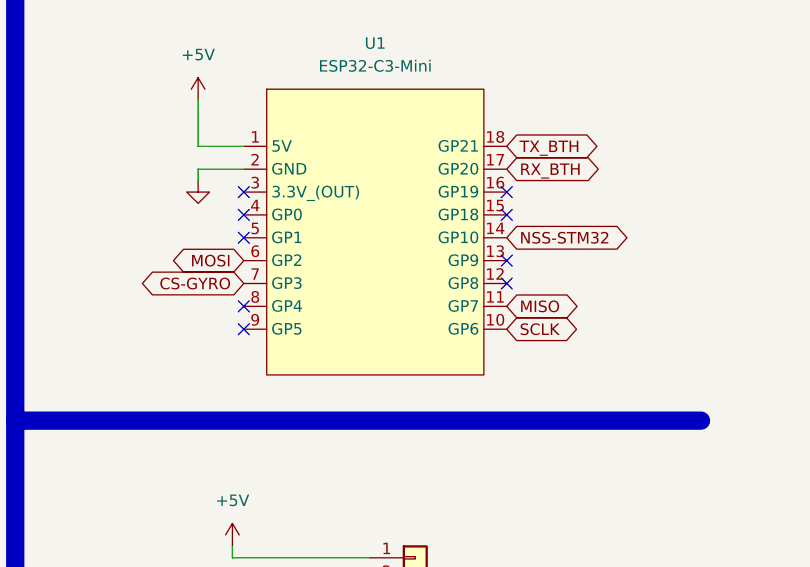
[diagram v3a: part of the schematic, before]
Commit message: pcb trace complete
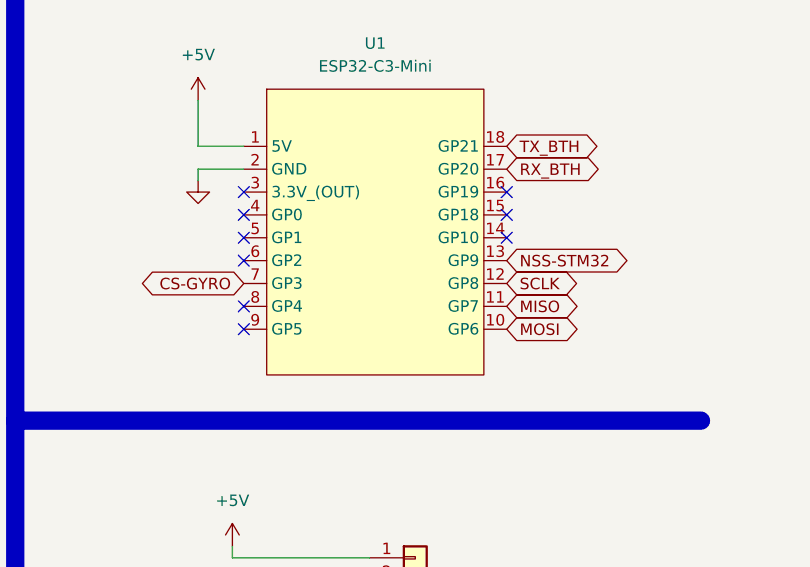
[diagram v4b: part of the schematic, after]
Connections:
- net MOSI: now also U1.10 (GP6); no longer U1.6 (GP2)
- net NSS-STM32: now also U1.13 (GP9); no longer U1.14 (GP10)
- net SCLK: now also U1.12 (GP8); no longer U1.10 (GP6)
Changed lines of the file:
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@@
 	)
 	(no_connect
-		(at 560.07 60.96)
-	)
-	(no_connect
 		(at 450.85 78.74)
 	)
@@
 	)
 	(no_connect
+		(at 560.07 55.88)
+	)
+	(no_connect
 		(at 530.86 66.04)
 	)
@@
 	)
 	(no_connect
-		(at 560.07 58.42)
+		(at 530.86 58.42)
 	)
 	(no_connect
@@
 	(global_label "NSS-STM32"
 		(shape bidirectional)
-		(at 560.07 55.88 0)
+		(at 560.07 58.42 0)
 		(fields_autoplaced yes)
 		(effects
@@
 		)
 		(property "Intersheetrefs" "${INTERSHEET_REFS}"
-			(at 575.5359 55.88 0)
+			(at 575.5359 58.42 0)
 			(effects
 				(font
@@
 	(global_label "SCLK"
 		(shape bidirectional)
-		(at 560.07 66.04 0)
+		(at 560.07 60.96 0)
 		(fields_autoplaced yes)
 		(effects
@@
 		)
 		(property "Intersheetrefs" "${INTERSHEET_REFS}"
-			(at 568.9441 66.04 0)
+			(at 568.9441 60.96 0)
 			(effects
 				(font
@@
 	(global_label "MOSI"
 		(shape bidirectional)
-		(at 530.86 58.42 180)
+		(at 560.07 66.04 0)
 		(fields_autoplaced yes)
 		(effects
@@
 				(size 1.27 1.27)
 			)
-			(justify right)
+			(justify left)
 		)
 		(property "Intersheetrefs" "${INTERSHEET_REFS}"
-			(at 522.1673 58.42 0)
+			(at 568.7627 66.04 0)
 			(effects
 				(font
 					(size 1.27 1.27)
 				)
-				(justify right)
+				(justify left)
 				(hide yes)
 			)

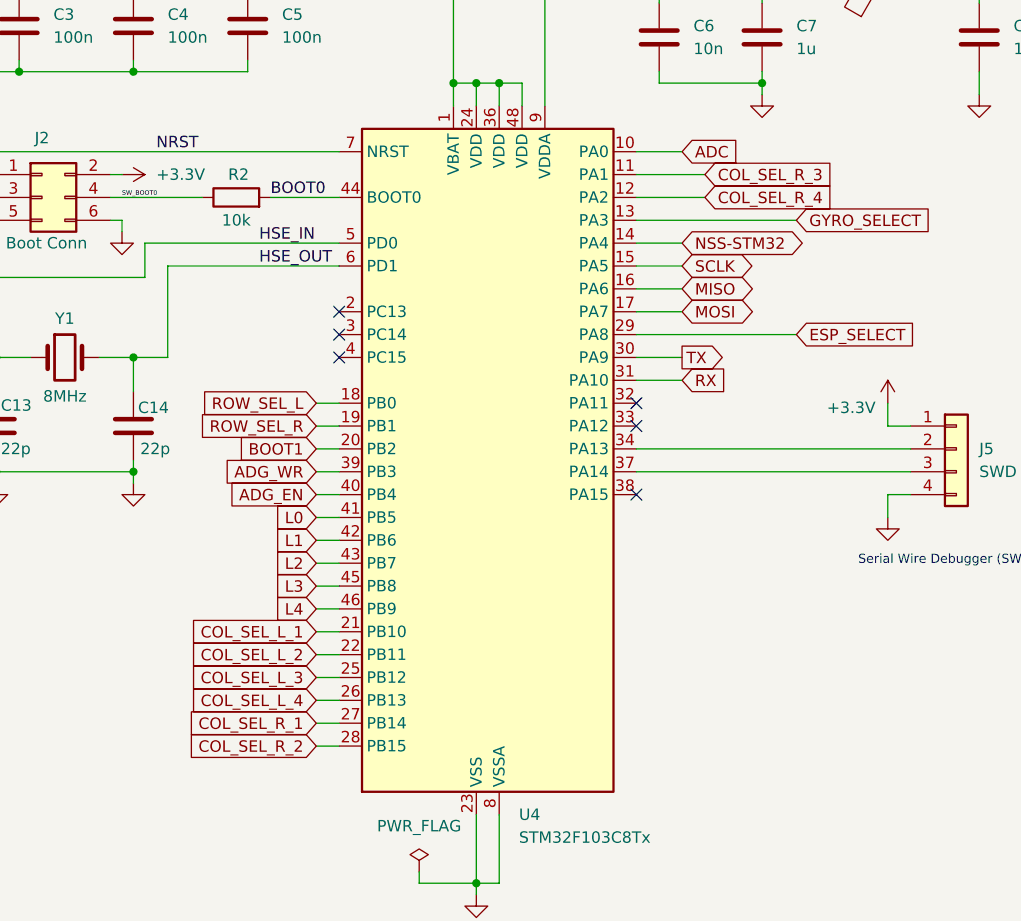
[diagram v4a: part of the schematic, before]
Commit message: re-configured the pins connection again
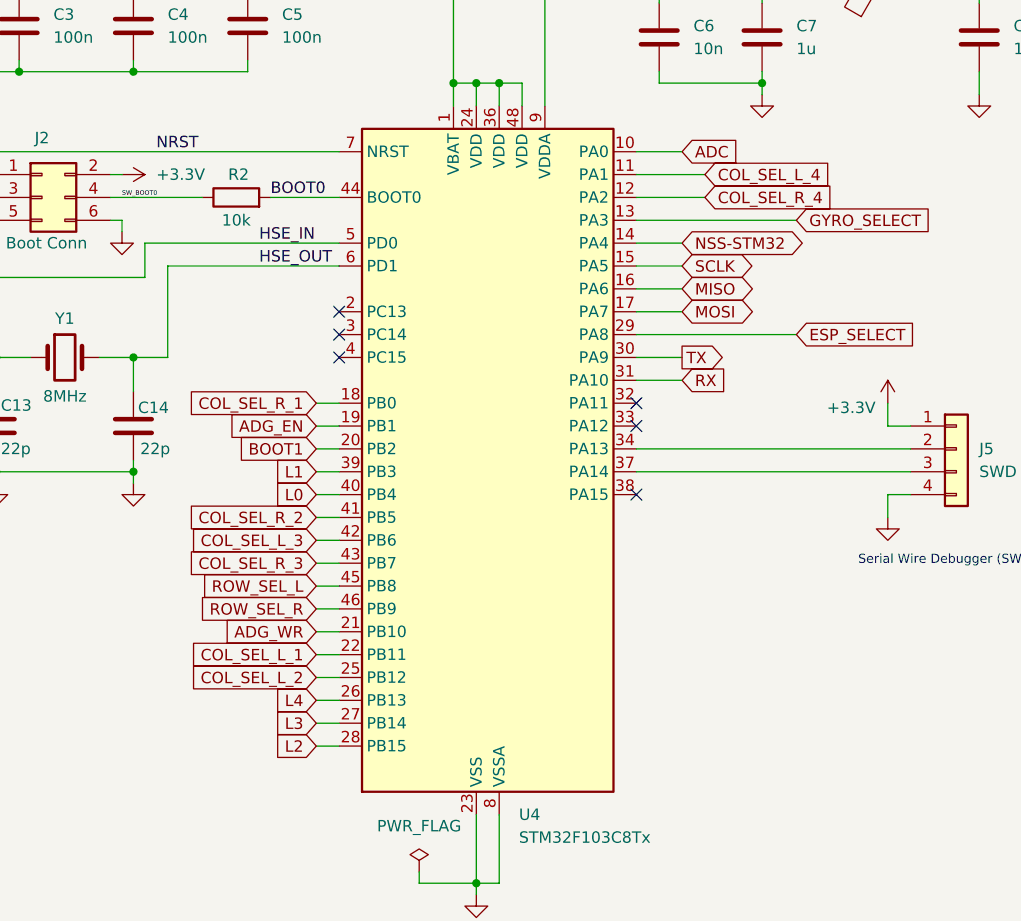
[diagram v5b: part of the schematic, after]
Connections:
- net ADG_EN: now also U4.19 (PB1); no longer U4.40 (PB4)
- net ADG_WR: now also U4.21 (PB10); no longer U4.39 (PB3)
- net COL_SEL_L_1: now also U4.22 (PB11); no longer U4.21 (PB10)
- net COL_SEL_L_2: now also U4.25 (PB12); no longer U4.22 (PB11)
- net COL_SEL_L_3: now also U4.42 (PB6); no longer U4.25 (PB12)
- net COL_SEL_L_4: now also U4.11 (PA1); no longer U4.26 (PB13)
- net COL_SEL_R_1: now also U4.18 (PB0); no longer U4.27 (PB14)
- net COL_SEL_R_2: now also U4.41 (PB5); no longer U4.28 (PB15)
- net COL_SEL_R_3: now also U4.43 (PB7); no longer U4.11 (PA1)
- net L0: now also U4.40 (PB4); no longer U4.41 (PB5)
- net L1: now also U4.39 (PB3); no longer U4.42 (PB6)
- net L2: now also U4.28 (PB15); no longer U4.43 (PB7)
- net L3: now also U4.27 (PB14); no longer U4.45 (PB8)
- net L4: now also U4.26 (PB13); no longer U4.46 (PB9)
- net ROW_SEL_L: now also U4.45 (PB8); no longer U4.18 (PB0)
- net ROW_SEL_R: now also U4.46 (PB9); no longer U4.19 (PB1)

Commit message: bluetooth module has removed
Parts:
- added J18: Conn_01x02, Connector_PinHeader_2.54mm:PinHeader_1x02_P2.54mm_Vertical, symbol Connector_Generic:Conn_01x02
- J1, J3, J4: now not fitted; now left out of the parts list
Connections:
- net CS-GYRO: now also U1.9 (GP5); no longer U1.7 (GP3)
- net MISO: now also U1.7 (GP3); no longer U1.11 (GP7)
- net MOSI: now also U1.8 (GP4); no longer U1.10 (GP6)
- net NSS-STM32: now also U1.5 (GP1); no longer U1.13 (GP9)
- net RX: now also U2.1 (TXD)
- net RX_USB: no longer U2.5 (RXD)
- net SCLK: now also U1.6 (GP2); no longer U1.12 (GP8)
- net TX: now also U2.5 (RXD)
- net TX_USB: no longer U2.1 (TXD)
- net SENSOR_OUT renamed SENSOR_OUT_R
- net SENSOR_OUT_R: now also J18.1 (Pin_1); no longer U6.43 (D)
- new net SENSOR_OUT_L: J18.2 (Pin_2), U6.43 (D)
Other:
- note added: "GYRO Moule"
- note added: "Gain Controller"
- note added: "Multiplexers: Switching Circuits"
- note added: "Sensor Processor STM32F103C8T6"
- note added: "Shorted by Jumpper"
- note added: "USB to UART"
- note added: "WiFi Module"
